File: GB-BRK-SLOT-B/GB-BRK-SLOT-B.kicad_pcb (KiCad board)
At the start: 2 copper layers, 81 x 80 mm, 24 parts, among them J1 Conn_02x16_Odd_Even, J2 Conn_02x16_Odd_Even, J3 GameBoy_Cartridge, J4 Conn_02x02_Odd_Even

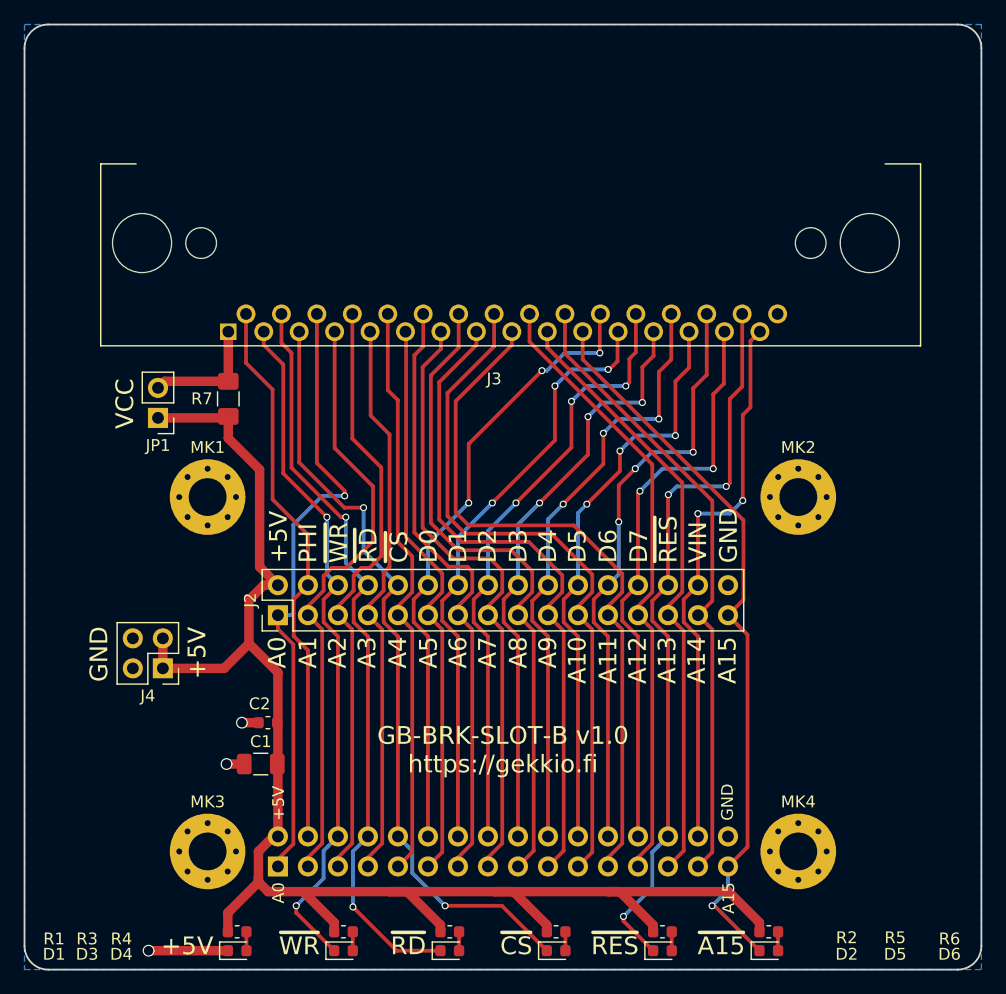
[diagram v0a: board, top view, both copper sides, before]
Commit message: Upgrade most projects to KiCad 6
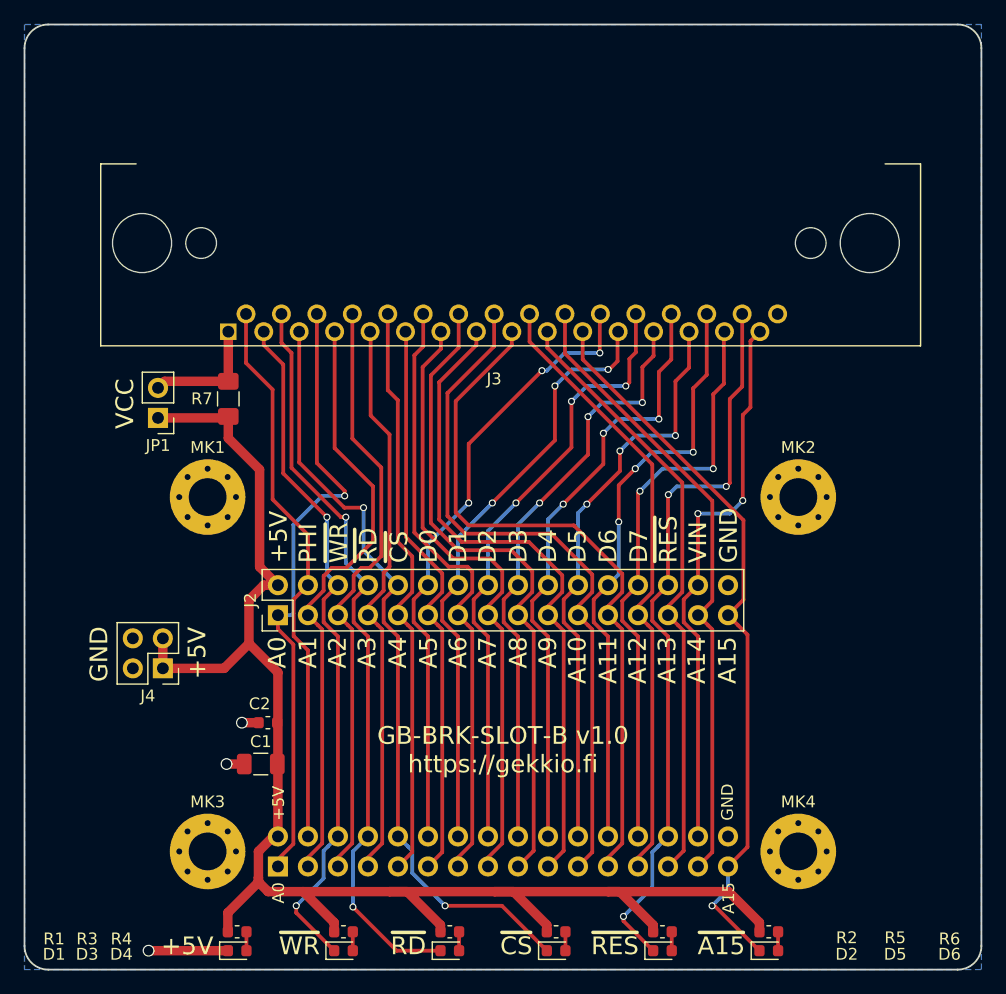
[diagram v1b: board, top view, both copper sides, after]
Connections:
- net /~CS renamed /~{CS}
- net /~RD renamed /~{RD}
- net /~RES renamed /~{RES}
- net /~WR renamed /~{WR}
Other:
- net class Default removed
- net class Power removed
- board text added: "~{A15}"
- board text added: "~{CS}"
- board text added: "~{RD}"
- board text added: "~{RES}"
- board text added: "~{WR}"
- board text removed: "~A15"
- board text removed: "~CS"
- board text removed: "~RD"
- board text removed: "~RES"
- board text removed: "~WR"
